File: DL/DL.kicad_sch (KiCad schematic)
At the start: 3 parts, among them J1 Rpi_l(0-15), J2 Rpi_r, J3 SD_Card

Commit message: Add files via upload
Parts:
- added C1: 100n, Capacitor_SMD:C_0805_2012Metric_Pad1.18x1.45mm_HandSolder, symbol Device:C
- added IC?: SCD42-D-R2, SCD42DR2, symbol SCD42-D-R2:SCD42-D-R2
- added IC?: TGS3870-B00, TGS3870B00, symbol TGS3870-B00:TGS3870-B00
- added U1: SHT31-DIS, Sensor_Humidity:Sensirion_DFN-8-1EP_2.5x2.5mm_P0.5mm_EP1.1x1.7mm, symbol Sensor_Humidity:SHT31-DIS
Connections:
- net GND: now also J2.3 (Pin_3), C1.2, U1.2 (ADDR), U1.7 (R), U1.8 (VSS), U1.9 (VSS)
- net GP2/SPI_SCK0/SDA1: now also U1.1 (SDA)
- net GP3/SPI_TX0/I2C_SDA1 renamed GP3/SPI_TX0/I2C_SCL1
- net GP3/SPI_TX0/I2C_SCL1: now also U1.4 (SCL)
- new net: C1.1, U1.5 (VDD)
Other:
- note added: "SHT31-DIS"
- moved on the sheet: J3

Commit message: All sensors wiring
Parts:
- added C1: 1u, Capacitor_SMD:C_0805_2012Metric_Pad1.18x1.45mm_HandSolder, symbol Device:C
- added IC1: MCP6V96UT-E_OT, SOT95P280X145-5N, symbol MCP6V96UT-E_OT:MCP6V96UT-E_OT
- added R1: 1M, Resistor_SMD:R_0805_2012Metric_Pad1.20x1.40mm_HandSolder, symbol Device:R
- added R2: 1k, symbol Device:R
- added U2: TGS5141-P00, Figaro-TGS5141-P00-*, symbol TGS5141-P00:TGS5141-P00
- gave numbers to parts that had none: 2
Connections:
- net 3V3_OUT is gone; now on net +3.3V: J2.5 (Pin_5)
- net GND: now also IC2.20 (GND_2), IC2.21 (GND_3), IC2.6 (GND_1), IC3.1 (COMMON(-)), IC1.2 (VSS), IC1.3 (VIN-), U2.2 (Counter)
- net GP26/ADC0/I2C_SDA1: now also IC3.2 (SENSOR_ELECTRODE_(+)), C1.2, IC1.4 (VOUT), R1.2, R2.2
- net GP2/SPI_SCK0/SDA1: now also IC2.10 (SDA)
- net GP3/SPI_TX0/I2C_SCL1: now also IC2.9 (SCL)
- net +3.3V: now reaches IC2.7 (VDD)
- net +3.3V: now also C1.1, U1.5 (VDD), IC1.5 (VDD)
- net VD: now reaches IC3.3 (HEATER(+))
- new net: C1.1, IC1.1 (VIN+), R1.1, U2.1 (Working)
- new net +5V: R2.1
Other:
- note added: "TGS5141-P00"
- moved on the sheet: IC2, IC3, J3

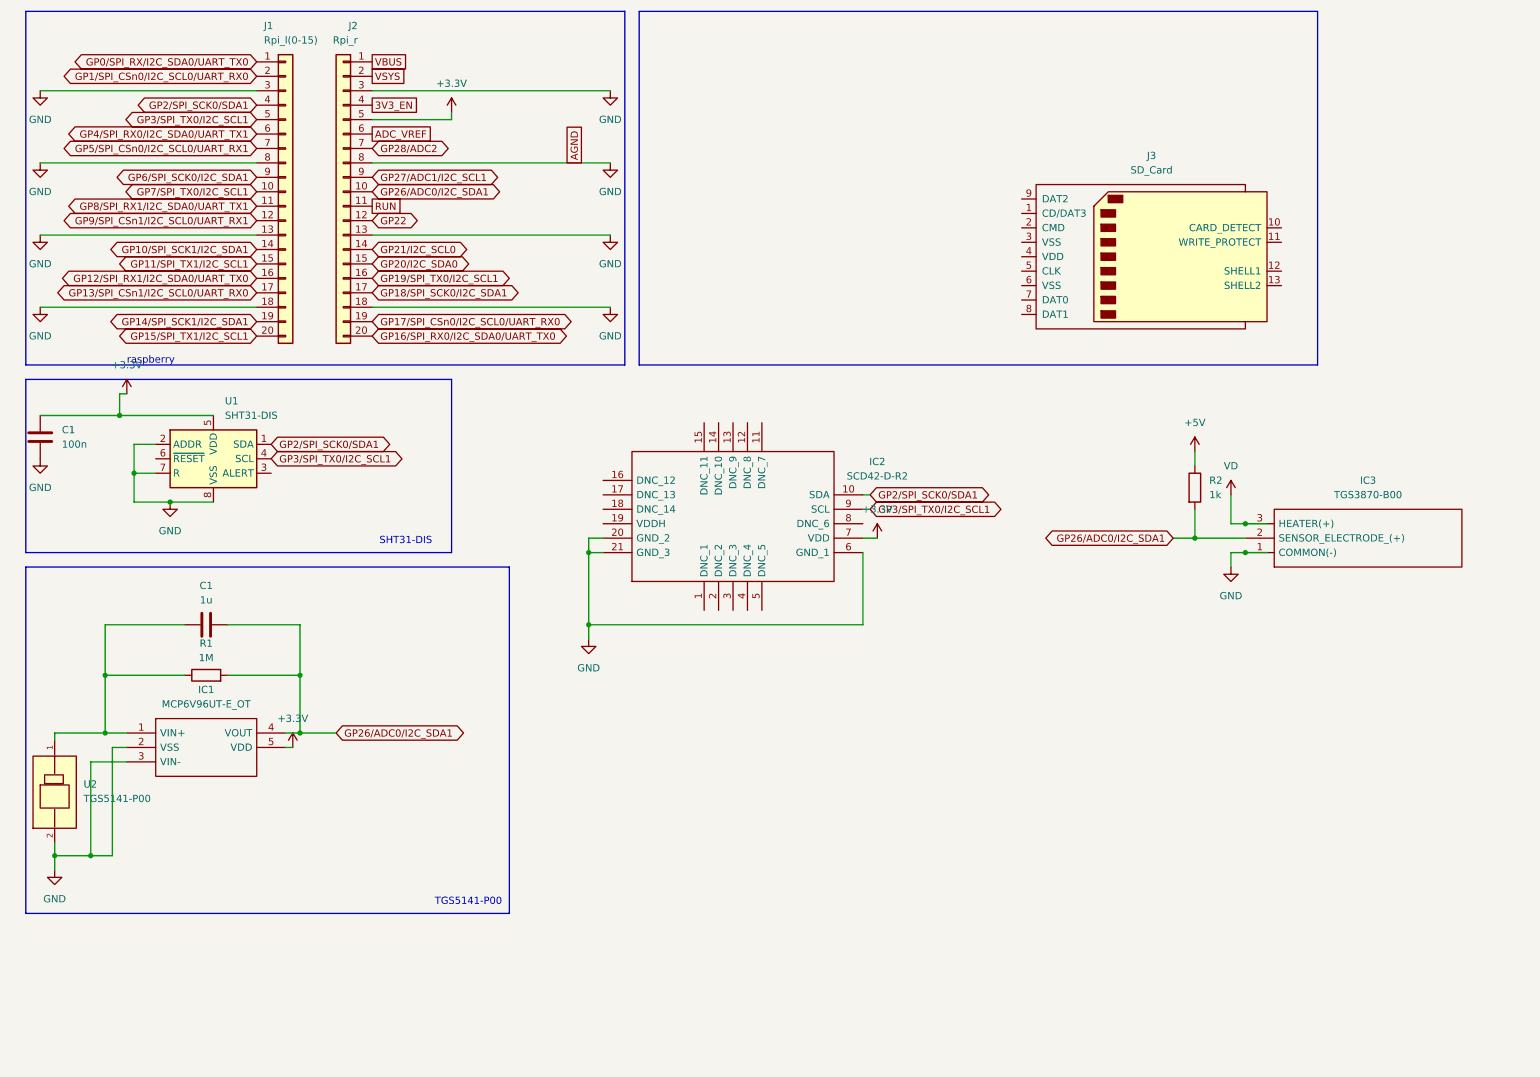
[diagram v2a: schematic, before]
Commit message: Complete electric scheme
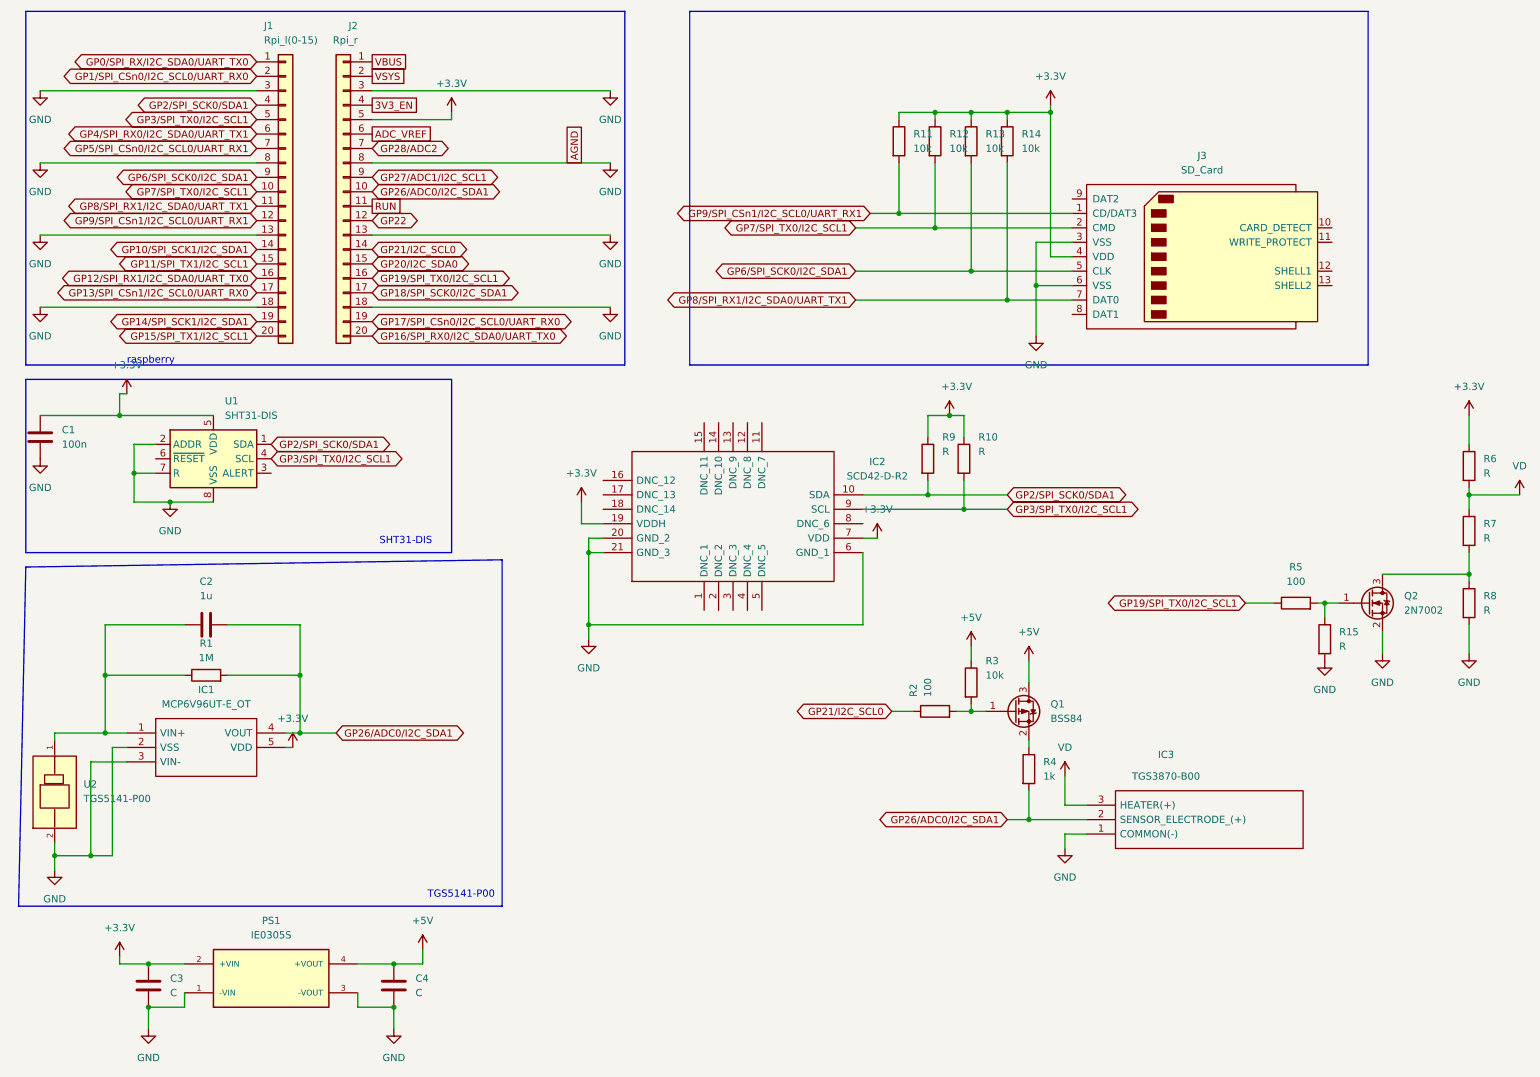
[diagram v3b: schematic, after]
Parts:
- added C3, C4: C, symbol Device:C
- added PS1: IE0305S, CONV_IE0305S, symbol IE0305S:IE0305S
- added Q1: BSS84, Package_TO_SOT_SMD:SOT-23, symbol Transistor_FET:BSS84
- added Q2: 2N7002, Package_TO_SOT_SMD:SOT-23, symbol Transistor_FET:2N7002
- added R10, R9: R, Resistor_SMD:R_0805_2012Metric, symbol Device:R
- added R11, R12, R13, R14: 10k, symbol Device:R
- added R15, R6, R7, R8: R, symbol Device:R
- added R2: 100, Resistor_SMD:R_0805_2012Metric, symbol Device:R
- added R3: 10k, Resistor_SMD:R_0805_2012Metric, symbol Device:R
- added R5: 100, symbol Device:R
- renumbered C1 to C2, R2 to R4
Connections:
- net +3.3V: now also IC2.19 (VDDH), J3.4 (VDD), C3.1, PS1.2 (+VIN), R10.1, R11.1, R12.1, R13.1, R14.1, R6.1, R9.1
- net +5V: now also C4.1, PS1.4 (+VOUT), Q1.3 (D), R3.1; no longer R4.1
- net GND: now also J3.3 (VSS), J3.6 (VSS), C3.2, C4.2, PS1.1 (-VIN), PS1.3 (-VOUT), Q2.2 (S), R15.2, R8.2
- net GP19/SPI_TX0/I2C_SCL1: now also R5.1
- net GP21/I2C_SCL0: now also R2.1
- net GP2/SPI_SCK0/SDA1: now also R9.2
- net GP3/SPI_TX0/I2C_SCL1: now also R10.2
- net GP6/SPI_SCK0/I2C_SDA1: now also J3.5 (CLK), R13.2
- net GP7/SPI_TX0/I2C_SCL1: now also J3.2 (CMD), R12.2
- net GP8/SPI_RX1/I2C_SDA0/UART_TX1: now also J3.7 (DAT0), R14.2
- net GP9/SPI_CSn1/I2C_SCL0/UART_RX1: now also J3.1 (CD/DAT3), R11.2
- net VD: now also R6.2, R7.1
- new net: Q2.3 (D), R7.2, R8.1
- new net: Q2.1 (G), R15.1, R5.2
- new net: Q1.2 (S), R4.1
- new net: Q1.1 (G), R2.2, R3.2
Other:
- moved on the sheet: IC3, J3, R4

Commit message: PCB layout interation no. 1
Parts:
- removed J1: Rpi_l(0-15), Connector_PinSocket_2.54mm:PinSocket_1x20_P2.54mm_Vertical, symbol Connector_Generic:Conn_01x20
- removed J2: Rpi_r, Connector_PinSocket_2.54mm:PinSocket_1x20_P2.54mm_Vertical, symbol Connector_Generic:Conn_01x20
- added BZ1: Buzzer, symbol Device:Buzzer
- added J4, J5, J6, J7: Conn_01x05_Male, Connector_Wire:SolderWire-1sqmm_1x05_P7.8mm_D1.4mm_OD3.9mm, symbol Connector:Conn_01x05_Male
- added R16, R17, R18, R19, R20: R, Resistor_SMD:R_0805_2012Metric_Pad1.20x1.40mm_HandSolder, symbol Device:R
- added U3: Pico, MCU_RaspberryPi_and_Boards:RPi_Pico_SMD_TH, symbol MCU_RaspberryPi_and_Boards:Pico
- C3, C4: footprint (none) -> Capacitor_SMD:C_0805_2012Metric_Pad1.18x1.45mm_HandSolder
- IC1: footprint SOT95P280X145-5N -> MCP6V96UT-E_OT:SOT95P280X145-5N
- IC2: footprint SCD42DR2 -> SCD42-D-R2:SCD42DR2
- IC3: footprint TGS3870B00 -> TGS3870-B00:TGS3870B00
- PS1: footprint CONV_IE0305S -> IE0305S:CONV_IE0305S
- R10, R9: value R -> 10k; footprint Resistor_SMD:R_0805_2012Metric -> Resistor_SMD:R_0805_2012Metric_Pad1.20x1.40mm_HandSolder
- R11, R12, R13, R14, R4, R5, R6, R7, R8: footprint (none) -> Resistor_SMD:R_0805_2012Metric_Pad1.20x1.40mm_HandSolder
- R15: value R -> 10k; footprint (none) -> Resistor_SMD:R_0805_2012Metric_Pad1.20x1.40mm_HandSolder
- R2, R3: footprint Resistor_SMD:R_0805_2012Metric -> Resistor_SMD:R_0805_2012Metric_Pad1.20x1.40mm_HandSolder
- U2: footprint Figaro-TGS5141-P00-* -> TGS5141-P00:Figaro-TGS5141-P00-MFG
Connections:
- net +3.3V: now also J5.1 (Pin_1), J5.2 (Pin_2), J5.3 (Pin_3), J5.4 (Pin_4), J5.5 (Pin_5), U3.36 (3V3)
- net 3V3_EN: now also U3.37 (3V3_EN)
- net ADC_VREF: now also U3.35 (ADC_VREF)
- net GND: now also J3.12 (SHELL1), J3.13 (SHELL2), BZ1.2 (+), J6.1 (Pin_1), J6.2 (Pin_2), J6.3 (Pin_3), J6.4 (Pin_4), J6.5 (Pin_5), U3.13 (GND), U3.18 (GND), U3.23 (GND), U3.28 (GND), U3.3 (GND), U3.33 (AGND), U3.38 (GND), U3.8 (GND)
- net GP0/SPI_RX/I2C_SDA0/UART_TX0: now also U3.1 (GPIO0)
- net GP10/SPI_SCK1/I2C_SDA1: now also R20.2, U3.14 (GPIO10)
- net GP11/SPI_TX1/I2C_SCL1: now also R19.2, U3.15 (GPIO11)
- net GP12/SPI_RX1/I2C_SDA0/UART_TX0: now also R18.2, U3.16 (GPIO12)
- net GP13/SPI_CSn1/I2C_SCL0/UART_RX0: now also R17.2, U3.17 (GPIO13)
- net GP14/SPI_SCK1/I2C_SDA1: now also R16.2, U3.19 (GPIO14)
- net GP15/SPI_TX1/I2C_SCL1: now also BZ1.1 (-), U3.20 (GPIO15)
- net GP16/SPI_RX0/I2C_SDA0/UART_TX0: now also J7.5 (Pin_5), U3.21 (GPIO16)
- net GP17/SPI_CSn0/I2C_SCL0/UART_RX0: now also J7.4 (Pin_4), U3.22 (GPIO17)
- net GP18/SPI_SCK0/I2C_SDA1: now also J7.3 (Pin_3), U3.24 (GPIO18)
- net GP19/SPI_TX0/I2C_SCL1: now also U3.25 (GPIO19)
- net GP1/SPI_CSn0/I2C_SCL0/UART_RX0: now also U3.2 (GPIO1)
- net GP20/I2C_SDA0: now also J7.2 (Pin_2), U3.26 (GPIO20)
- net GP21/I2C_SCL0: now also U3.27 (GPIO21)
- net GP22: now also J7.1 (Pin_1), U3.29 (GPIO22)
- net GP26/ADC0/I2C_SDA1: now also U3.31 (GPIO26_ADC0); no longer IC3.2 (SENSOR_ELECTRODE_(+)), R4.2
- net GP27/ADC1/I2C_SCL1: now also IC3.2 (SENSOR_ELECTRODE_(+)), R4.2, U3.32 (GPIO27_ADC1)
- net GP28/ADC2: now also U3.34 (GPIO28_ADC2)
- net GP2/SPI_SCK0/SDA1: now also U3.4 (GPIO2)
- net GP3/SPI_TX0/I2C_SCL1: now also U3.5 (GPIO3)
- net GP4/SPI_RX0/I2C_SDA0/UART_TX1: now also U3.6 (GPIO4)
- net GP5/SPI_CSn0/I2C_SCL0/UART_RX1: now also U3.7 (GPIO5)
- net GP6/SPI_SCK0/I2C_SDA1: now also U3.9 (GPIO6)
- net GP7/SPI_TX0/I2C_SCL1: now also U3.10 (GPIO7)
- net GP8/SPI_RX1/I2C_SDA0/UART_TX1: now also U3.11 (GPIO8)
- net GP9/SPI_CSn1/I2C_SCL0/UART_RX1: now also U3.12 (GPIO9)
- net RUN: now also U3.30 (RUN)
- net VBUS: now also U3.40 (VBUS)
- net VSYS: now also U3.39 (VSYS)
- new net: J4.1 (Pin_1), R16.1
- new net: J4.2 (Pin_2), R17.1
- new net: J4.3 (Pin_3), R18.1
- new net: J4.4 (Pin_4), R19.1
- new net: J4.5 (Pin_5), R20.1
- no-connect marks 0 -> 24
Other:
- moved on the sheet: C3, C4, IC2, IC3, J3, PS1, Q1, Q2, R10, R11, R12, R13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

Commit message: PCB layout interation no. 2
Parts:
- BZ1: footprint (none) -> Buzzer_Beeper:Buzzer_12x9.5RM7.6
- J4, J5, J6, J7: footprint Connector_Wire:SolderWire-1sqmm_1x05_P7.8mm_D1.4mm_OD3.9mm -> Connector_PinHeader_2.54mm:PinHeader_1x05_P2.54mm_Vertical
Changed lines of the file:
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@@
     (property "Reference" "J7" (id 0) (at 161.29 226.06 0))
     (property "Value" "Conn_01x05_Male" (id 1) (at 161.29 228.6 0))
-    (property "Footprint" "Connector_Wire:SolderWire-1sqmm_1x05_P7.8mm_D1.4mm_OD3.9mm" (id 2) (at 156.21 217.17 0)
+    (property "Footprint" "Connector_PinHeader_2.54mm:PinHeader_1x05_P2.54mm_Vertical" (id 2) (at 156.21 217.17 0)
       (effects (font (size 1.27 1.27)) hide)
     )
@@
     (property "Reference" "J4" (id 0) (at 163.83 189.23 0))
     (property "Value" "Conn_01x05_Male" (id 1) (at 165.1 191.77 0))
-    (property "Footprint" "Connector_Wire:SolderWire-1sqmm_1x05_P7.8mm_D1.4mm_OD3.9mm" (id 2) (at 156.21 199.39 0)
+    (property "Footprint" "Connector_PinHeader_2.54mm:PinHeader_1x05_P2.54mm_Vertical" (id 2) (at 156.21 199.39 0)
       (effects (font (size 1.27 1.27)) hide)
     )
@@
       (effects (font (size 1.27 1.27)) (justify right))
     )
-    (property "Footprint" "Connector_Wire:SolderWire-1sqmm_1x05_P7.8mm_D1.4mm_OD3.9mm" (id 2) (at 153.67 217.17 0)
+    (property "Footprint" "Connector_PinHeader_2.54mm:PinHeader_1x05_P2.54mm_Vertical" (id 2) (at 153.67 217.17 0)
       (effects (font (size 1.27 1.27)) hide)
     )
@@
       (effects (font (size 1.27 1.27)) (justify left))
     )
-    (property "Footprint" "" (id 2) (at 131.445 195.58 90)
+    (property "Footprint" "Buzzer_Beeper:Buzzer_12x9.5RM7.6" (id 2) (at 131.445 195.58 90)
       (effects (font (size 1.27 1.27)) hide)
     )
@@
       (effects (font (size 1.27 1.27)) (justify right))
     )
-    (property "Footprint" "Connector_Wire:SolderWire-1sqmm_1x05_P7.8mm_D1.4mm_OD3.9mm" (id 2) (at 153.67 199.39 0)
+    (property "Footprint" "Connector_PinHeader_2.54mm:PinHeader_1x05_P2.54mm_Vertical" (id 2) (at 153.67 199.39 0)
       (effects (font (size 1.27 1.27)) hide)
     )
@@
     )
     (path "/28a0d66b-225f-4687-8baa-de09bbae42c9"
-      (reference "J4") (unit 1) (value "Conn_01x05_Male") (footprint "Connector_Wire:SolderWire-1sqmm_1x05_P7.8mm_D1.4mm_OD3.9mm")
+      (reference "J4") (unit 1) (value "Conn_01x05_Male") (footprint "Connector_PinHeader_2.54mm:PinHeader_1x05_P2.54mm_Vertical")
     )
     (path "/dae455e4-a8af-446d-ab52-70704fff5030"
-      (reference "J5") (unit 1) (value "Conn_01x05_Male") (footprint "Connector_Wire:SolderWire-1sqmm_1x05_P7.8mm_D1.4mm_OD3.9mm")
+      (reference "J5") (unit 1) (value "Conn_01x05_Male") (footprint "Connector_PinHeader_2.54mm:PinHeader_1x05_P2.54mm_Vertical")
     )
     (path "/29359ae9-8374-4a11-b0a3-dfa0d8e92e98"
-      (reference "J6") (unit 1) (value "Conn_01x05_Male") (footprint "Connector_Wire:SolderWire-1sqmm_1x05_P7.8mm_D1.4mm_OD3.9mm")
+      (reference "J6") (unit 1) (value "Conn_01x05_Male") (footprint "Connector_PinHeader_2.54mm:PinHeader_1x05_P2.54mm_Vertical")
     )
     (path "/26594f1e-3b5e-4021-8e0c-786418d248ea"
-      (reference "J7") (unit 1) (value "Conn_01x05_Male") (footprint "Connector_Wire:SolderWire-1sqmm_1x05_P7.8mm_D1.4mm_OD3.9mm")
+      (reference "J7") (unit 1) (value "Conn_01x05_Male") (footprint "Connector_PinHeader_2.54mm:PinHeader_1x05_P2.54mm_Vertical")
     )
     (path "/23340a14-6fb7-45a0-8140-5e7e3b27828d"
